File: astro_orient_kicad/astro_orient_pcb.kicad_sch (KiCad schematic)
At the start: 0 parts

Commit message: started creating schematic for PCB
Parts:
- added C1, C2, C4, C5: 2.2u, symbol Device:C_Small
- added C3, C6, C7, C8: 0.1u, symbol Device:C_Small
- added D1, D2, D3: SK6805, LED_SMD:LED_SK6812MINI_PLCC4_3.5x3.5mm_P1.75mm, symbol LED:SK6805
- added F1: Polyfuse, symbol Device:Polyfuse
- added J1: BME260, symbol Connector_Generic:Conn_01x07
- added J3: USB-C_Receptacle, UJ20-C-H-G-MSMT-9B-P16-TR:SAMESKY_UJ20-C-H-G-MSMT-9B-P16-TR, symbol custom_symbols:UJ20-C-H-G-MSMT-9B-P16-TR
- added R1, R2: R_Photo, symbol Device:R_Photo
- added R3, R4: 5.1k, symbol Device:R_US
- added R5, R6, R7: 10k, symbol Device:R_US
- added R8, R9: 470, symbol Device:R_US
- added SW1: SW_SPST, symbol Switch:SW_SPST
- added SW2: SW_Reset, symbol Switch:SW_Push_Open_Dual
- added U1: STM32F072CBTx, Package_QFP:LQFP-48_7x7mm_P0.5mm, symbol MCU_ST_STM32F0:STM32F072CBTx
- added U2: AP2112K-3.3, Package_TO_SOT_SMD:SOT-23-5, symbol Regulator_Linear:AP2112K-3.3
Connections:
- new net: J3.A5 (CC1), R3.2
- new net: D1.2 (DIN), R8.1
- new net: D1.4 (DOUT), R9.2
- new net: C3.2, R5.2, SW2.2, SW2.4, U1.7 (NRST)
- new net: J3.B5 (CC2), R4.2
- new net: F1.1, J3.A4_B9 (VBUS), J3.B4_A9 (VBUS_1)
- new net: F1.2, SW1.1 (A)
- new net +3.3V: C2.2, C4.2, J1.1 (Vin), R5.1, R6.1, R7.1, U2.5 (VOUT)
- new net +5V: C1.2, C5.2, C6.2, C7.2, C8.2, D1.3 (VDD), D2.3 (VDD), D3.3 (VDD), SW1.2 (B), U2.1 (VIN)
- new net GND: C1.1, C2.1, C3.1, C4.1, C5.1, C6.1, C7.1, C8.1, D1.1 (GND), D2.1 (GND), D3.1 (GND), J1.3 (GND), J3.A1_B12 (GND), J3.B1_A12 (GND_1), J3.SH1 (SHIELD), J3.SH2 (SHIELD_1), J3.SH3 (SHIELD_2), J3.SH4 (SHIELD_3), R1.1, R2.1, R3.1, R4.1, SW2.1, SW2.3, U1.23 (VSS), U1.35 (VSS), U1.47 (VSS), U1.8 (VSSA), U2.2 (GND)
- new net USB_D+: J3.A6 (DP1), J3.B6 (DP2), U1.33 (PA12)
- new net USB_D-: J3.A7 (DN1), J3.B7 (DN2), U1.32 (PA11)
- new net photoresis_1: R1.2, R6.2
- new net photoresis_2: R2.2, R7.2
- no-connect marks 0 -> 3

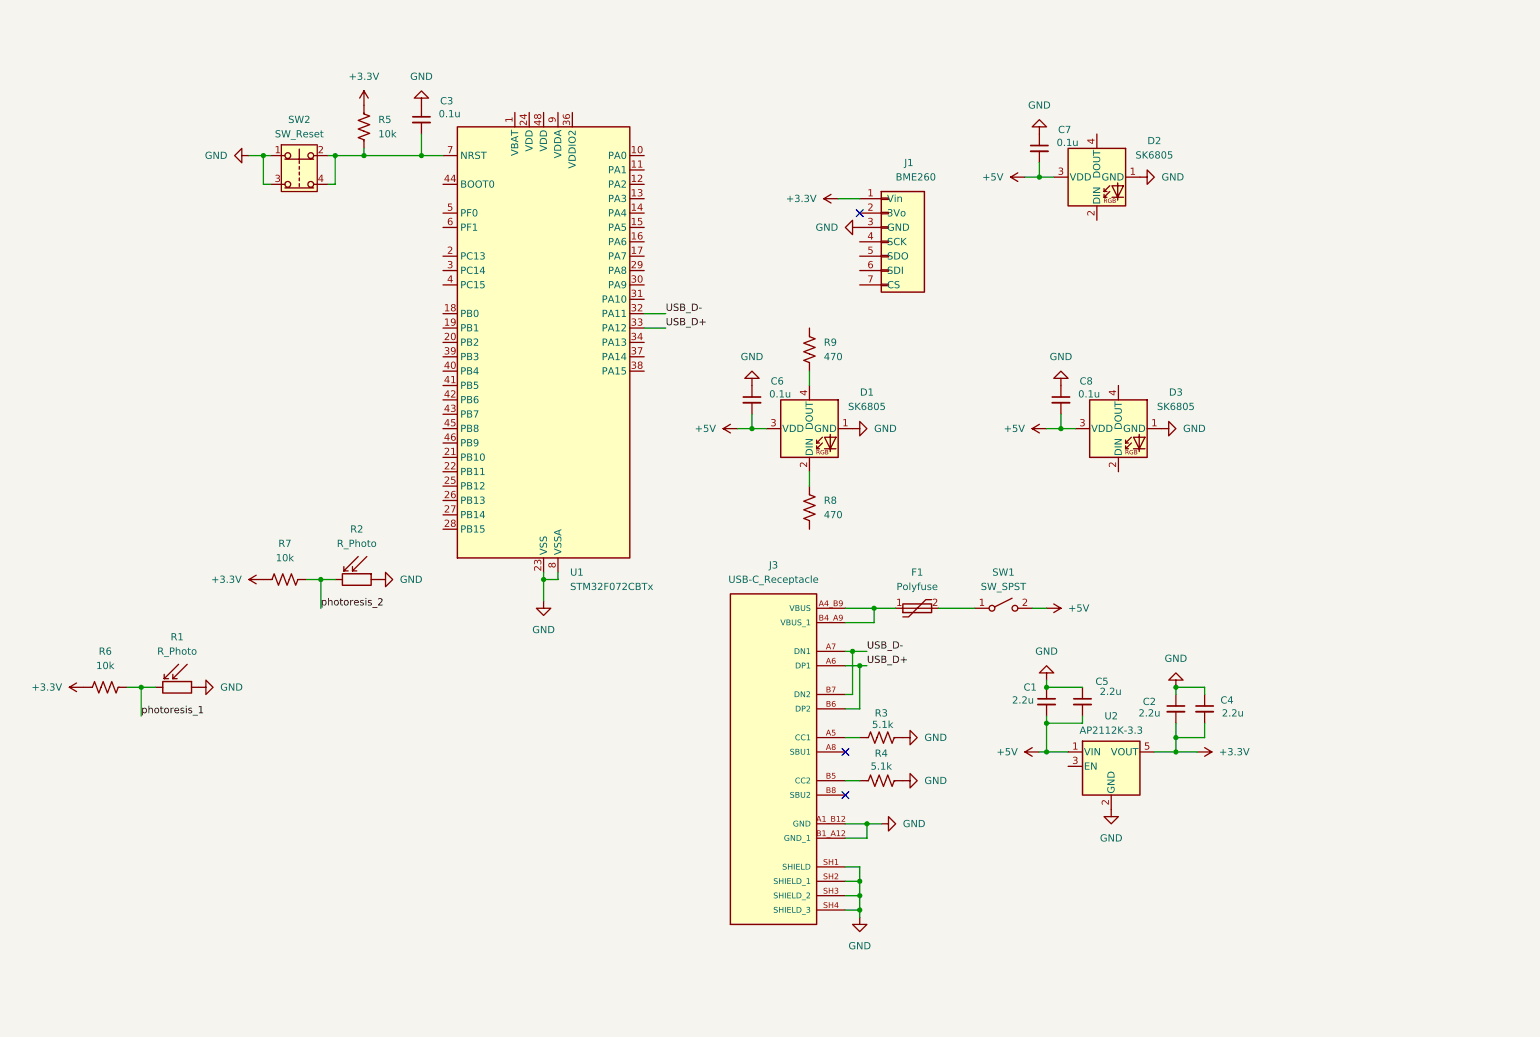
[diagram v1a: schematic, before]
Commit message: completed initial schematic, missing test pins
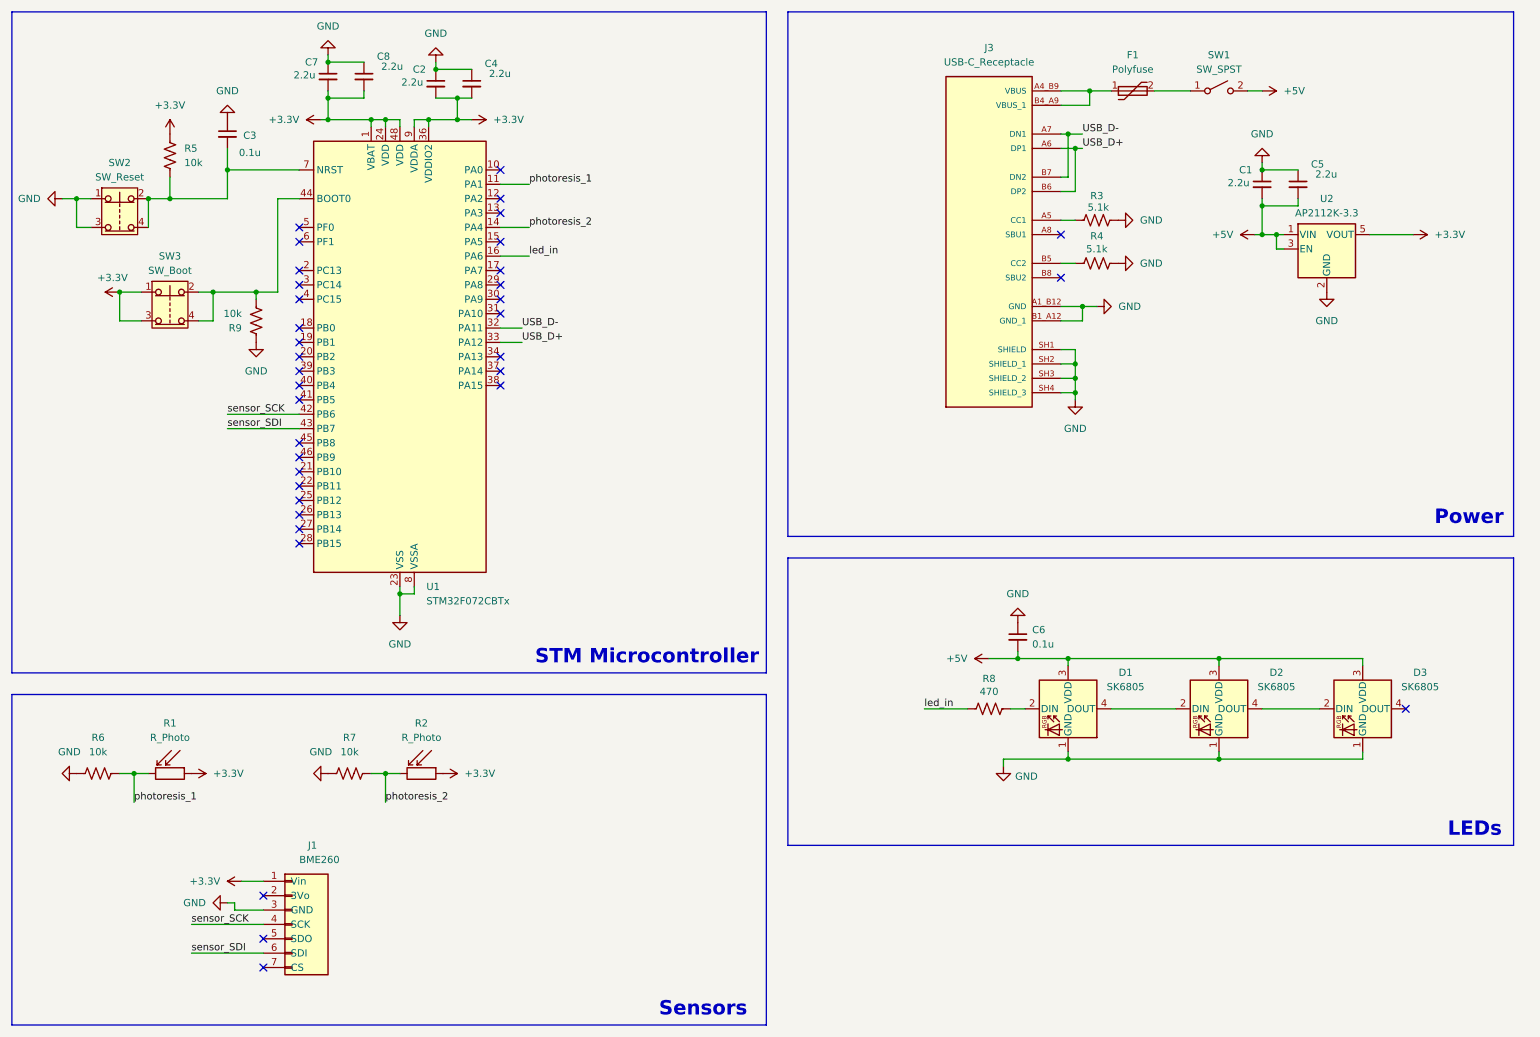
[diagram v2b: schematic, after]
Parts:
- added SW3: SW_Boot, symbol Switch:SW_Push_Open_Dual
- C7, C8: value 0.1u -> 2.2u
- R9: value 470 -> 10k
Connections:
- net +3.3V: now also C7.2, C8.2, R1.1, R2.1, U1.1 (VBAT), U1.24 (VDD), U1.36 (VDDIO2), U1.48 (VDD), U1.9 (VDDA), SW3.1, SW3.3; no longer R6.1, R7.1
- net +5V: now also U2.3 (EN); no longer C7.2, C8.2
- net GND: now also R6.1, R7.1, R9.1; no longer R1.1, R2.1
- net photoresis_1: now also U1.11 (PA1)
- net photoresis_2: now also U1.14 (PA4)
- net at D1.2 (DIN): now also R8.2; no longer R8.1
- net at R9.2: now also U1.44 (BOOT0), SW3.2, SW3.4; no longer D1.4 (DOUT)
- net led_in: now reaches U1.16 (PA6)
- net led_in: now also R8.1
- net sensor_SCK: now reaches U1.42 (PB6)
- net sensor_SCK: now also J1.4 (SCK)
- net sensor_SDI: now reaches U1.43 (PB7)
- net sensor_SDI: now also J1.6 (SDI)
- net at D2.2 (DIN): now also D1.4 (DOUT)
- net at D2.4 (DOUT): now also D3.2 (DIN)
- no-connect marks 3 -> 36
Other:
- note added: "LEDs"
- note added: "Power"
- note added: "STM Microcontroller"
- note added: "Sensors"
- moved on the sheet: C1, C3, C5, D1, D3, F1, J1, J3, R1, R2, R3, R4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

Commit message: Updated PCB schematic and created test files for GPS module
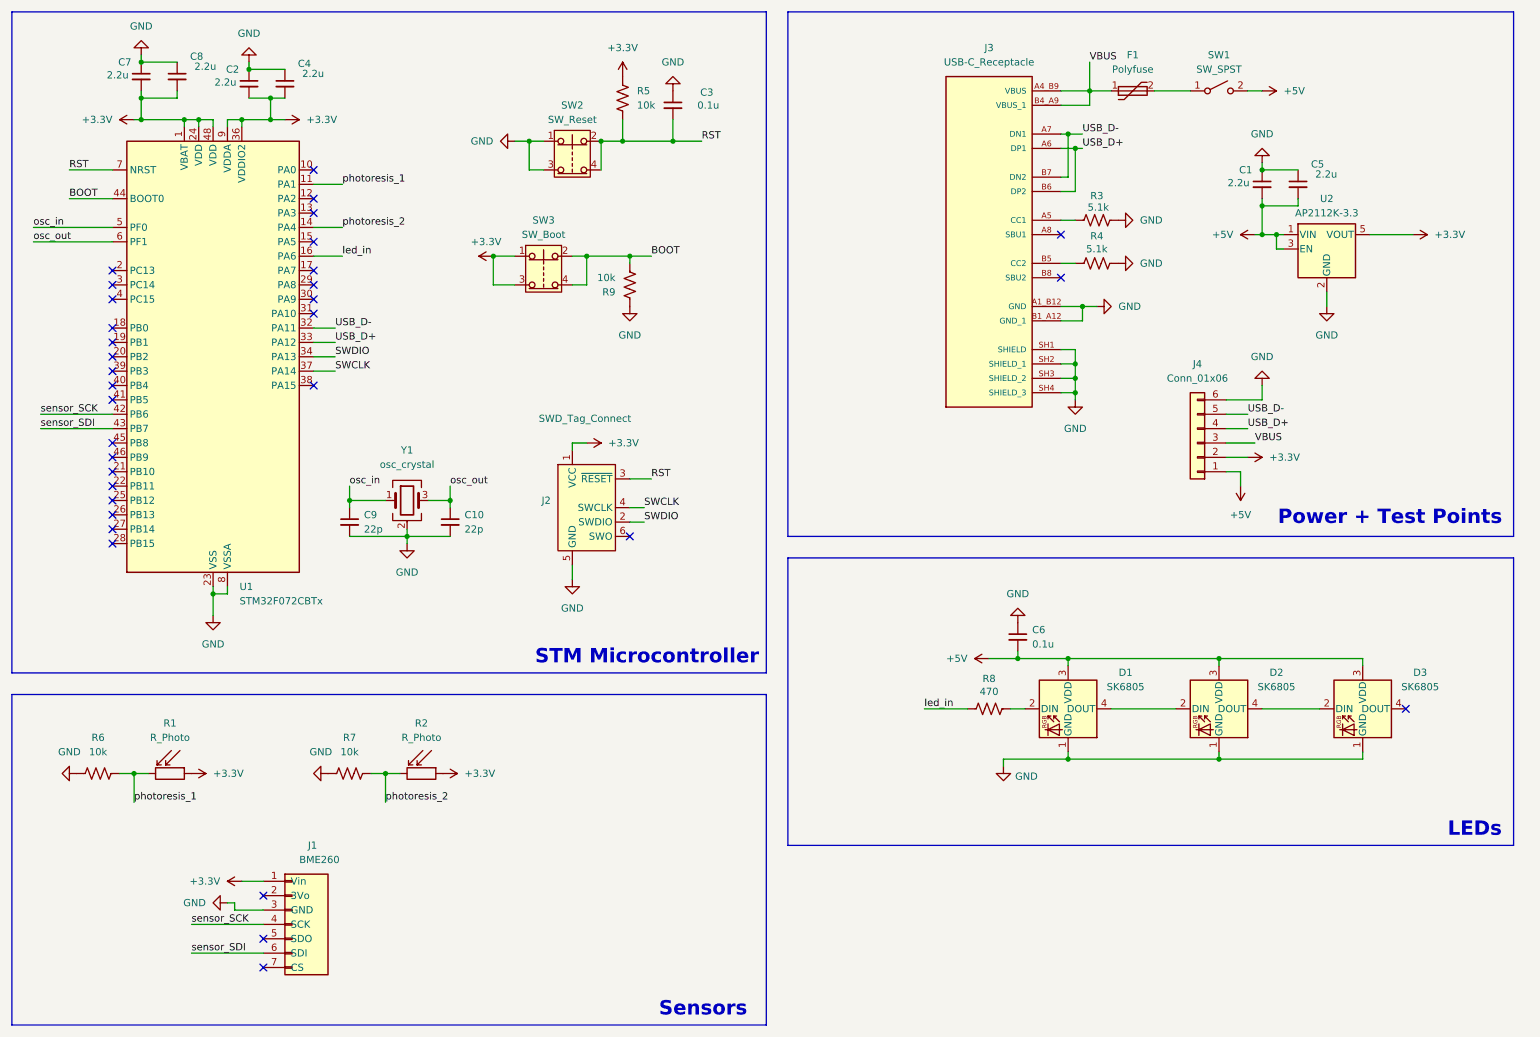
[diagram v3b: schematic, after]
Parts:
- added C10, C9: 22p, symbol Device:C_Small
- added J2: SWD_Tag_Connect, Connector:Tag-Connect_TC2030-IDC-FP_2x03_P1.27mm_Vertical, symbol Connector:Conn_ARM_SWD_TagConnect_TC2030
- added J4: Conn_01x06, symbol Connector_Generic:Conn_01x06
- added Y1: osc_crystal, symbol Device:Crystal_GND24
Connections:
- net +3.3V: now also J2.1 (VCC), J4.2 (Pin_2)
- net +5V: now also J4.1 (Pin_1)
- net GND: now also C10.2, C9.2, J2.5 (GND), J4.6 (Pin_6), Y1.2 (G), Y1.4 (G)
- net USB_D+: now also J4.4 (Pin_4)
- net USB_D-: now also J4.5 (Pin_5)
- net BOOT: now reaches R9.2, SW3.2, SW3.4, U1.44 (BOOT0)
- net SWDIO: now reaches U1.34 (PA13)
- net SWDIO: now also J2.2 (SWDIO)
- net SWCLK: now reaches U1.37 (PA14)
- net SWCLK: now also J2.4 (SWCLK)
- net osc_in: now reaches U1.5 (PF0)
- net osc_in: now also C9.1, Y1.1
- net osc_out: now reaches U1.6 (PF1)
- net osc_out: now also C10.1, Y1.3
- net RST: now reaches C3.2, R5.2, SW2.2, SW2.4, U1.7 (NRST)
- net RST: now also J2.3 (~{RESET})
- net VBUS: now reaches F1.1, J3.A4_B9 (VBUS), J3.B4_A9 (VBUS_1)
- net VBUS: now also J4.3 (Pin_3)
- no-connect marks 36 -> 33
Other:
- note added: "Power + Test Points"
- note removed: "Power"
- moved on the sheet: C2, C3, C4, C7, C8, R5, R9, SW2, SW3, U1

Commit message: Updated PCB schematic
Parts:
- J4: value Conn_01x06 -> test_points
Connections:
- net +3.3V: now also C5.2
- net +5V: no longer C5.2
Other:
- moved on the sheet: C5
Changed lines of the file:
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@@
 	)
 	(junction
-		(at 237.49 43.18)
-		(diameter 0)
-		(color 0 0 0 0)
-	)
-	(junction
 		(at 76.2 101.6)
 		(diameter 0)
@@
 	)
 	(junction
-		(at 237.49 49.53)
+		(at 204.47 39.37)
 		(diameter 0)
 		(color 0 0 0 0)
 	)
 	(junction
-		(at 204.47 39.37)
+		(at 120.65 38.1)
 		(diameter 0)
 		(color 0 0 0 0)
 	)
 	(junction
-		(at 120.65 38.1)
+		(at 262.89 54.61)
 		(diameter 0)
 		(color 0 0 0 0)
@@
 	(wire
 		(pts
-			(xy 237.49 43.18) (xy 243.84 43.18)
-		)
-		(stroke
-			(width 0)
-			(type default)
-		)
-	)
-	(wire
-		(pts
 			(xy 76.2 101.6) (xy 76.2 102.87)
 		)
@@
 	(wire
 		(pts
-			(xy 237.49 49.53) (xy 237.49 54.61)
+			(xy 237.49 48.26) (xy 237.49 54.61)
 		)
 		(stroke
@@
 	(wire
 		(pts
-			(xy 203.2 129.54) (xy 203.2 130.81)
+			(xy 262.89 41.91) (xy 262.89 43.18)
 		)
 		(stroke
@@
 	(wire
 		(pts
-			(xy 243.84 48.26) (xy 243.84 49.53)
+			(xy 203.2 129.54) (xy 203.2 130.81)
 		)
 		(stroke
@@
 	(wire
 		(pts
-			(xy 256.54 54.61) (xy 264.16 54.61)
-		)
-		(stroke
-			(width 0)
-			(type default)
-		)
-	)
-	(wire
-		(pts
-			(xy 237.49 48.26) (xy 237.49 49.53)
+			(xy 256.54 54.61) (xy 262.89 54.61)
 		)
 		(stroke
@@
 	(wire
 		(pts
-			(xy 133.35 38.1) (xy 138.43 38.1)
+			(xy 262.89 54.61) (xy 264.16 54.61)
 		)
 		(stroke
@@
 	(wire
 		(pts
-			(xy 118.11 63.5) (xy 118.11 58.42)
+			(xy 133.35 38.1) (xy 138.43 38.1)
 		)
 		(stroke
@@
 	(wire
 		(pts
-			(xy 52.07 121.92) (xy 52.07 118.11)
+			(xy 118.11 63.5) (xy 118.11 58.42)
 		)
 		(stroke
@@
 	(wire
 		(pts
-			(xy 69.85 58.42) (xy 74.93 58.42)
+			(xy 52.07 121.92) (xy 52.07 118.11)
 		)
 		(stroke
@@
 	(wire
 		(pts
-			(xy 243.84 49.53) (xy 237.49 49.53)
+			(xy 69.85 58.42) (xy 74.93 58.42)
 		)
 		(stroke
@@
 	(wire
 		(pts
+			(xy 262.89 48.26) (xy 262.89 54.61)
+		)
+		(stroke
+			(width 0)
+			(type default)
+		)
+	)
+	(wire
+		(pts
 			(xy 105.41 63.5) (xy 101.6 63.5)
 		)
@@
 			)
 		)
-		(property "Value" "Conn_01x06"
+		(property "Value" "test_points"
 			(at 226.06 80.01 0)
 			(effects
@@
 	(symbol
 		(lib_id "Device:C_Small")
-		(at 243.84 45.72 0)
+		(at 262.89 45.72 0)
 		(unit 1)
 		(exclude_from_sim no)
@@
 		(dnp no)
 		(property "Reference" "C5"
-			(at 246.126 42.164 0)
+			(at 265.176 42.164 0)
 			(effects
 				(font
@@
 		)
 		(property "Value" "2.2u"
-			(at 246.888 43.942 0)
+			(at 265.938 43.942 0)
 			(effects
 				(font
@@
 		)
 		(property "Footprint" ""
-			(at 243.84 45.72 0)
+			(at 262.89 45.72 0)
 			(effects
 				(font
@@
 		)
 		(property "Datasheet" "~"
-			(at 243.84 45.72 0)
+			(at 262.89 45.72 0)
 			(effects
 				(font
@@
 		)
 		(property "Description" "Unpolarized capacitor, small symbol"
-			(at 243.84 45.72 0)
+			(at 262.89 45.72 0)
 			(effects
 				(font
@@
 					(unit 1)
 				)
+			)
+		)
+	)
+	(symbol
+		(lib_id "power:GND")
+		(at 262.89 41.91 180)
+		(unit 1)
+		(exclude_from_sim no)
+		(in_bom yes)
+		(on_board yes)
+		(dnp no)
+		(fields_autoplaced yes)
+		(property "Reference" "#PWR035"
+			(at 262.89 35.56 0)
+			(effects
+				(font
+					(size 1.27 1.27)
+				)
+				(hide yes)
+			)
+		)
+		(property "Value" "GND"
+			(at 262.89 36.83 0)
+			(effects
+				(font
+					(size 1.27 1.27)
+				)
+			)
+		)
+		(property "Footprint" ""
+			(at 262.89 41.91 0)
+			(effects
+				(font
+					(size 1.27 1.27)
+				)
+				(hide yes)
+			)
+		)
+		(property "Datasheet" ""
+			(at 262.89 41.91 0)
+			(effects
+				(font
+					(size 1.27 1.27)
+				)
+				(hide yes)
+			)
+		)
+		(property "Description" "Power symbol creates a global label with name \"GND\" , ground"
+			(at 262.89 41.91 0)
+			(effects
+				(font
+					(size 1.27 1.27)
+				)
+				(hide yes)
+			)
+		)
+		(pin "1"
+		)
+		(instances
+			(project "astro_orient_pcb"
+				(path "/95adfdc0-de86-4f82-8c2e-667af04cb4ea"
+					(reference "#PWR035")
+					(unit 1)
+				)

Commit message: Updated PCB schematic
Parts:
- added C11: 0.1u, symbol Device:C_Small
- C2, C4, C7: value 2.2u -> 0.1u
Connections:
- net +3.3V: now also C11.2
- net GND: now also C11.1
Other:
- moved on the sheet: C10, C3, C7, C9, J2, R5, R9, SW2, SW3, U1, Y1
